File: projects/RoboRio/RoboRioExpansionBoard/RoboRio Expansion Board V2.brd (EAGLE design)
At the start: 56.6 x 77.5 mm, 125 parts, among them J1 RRINTERFACE-FEMALE, J10 SPI_MISO, J11 SPI_MOSI, J12 I2C_SCL, J13 I2C_SDA, J14 UART_TX, J15 UART_RX, J16 LCD, J17 ADC1, J18 ADC2, J19 ADC3, J2 MICROSD-HINGED, J20 ADC4, J21 ADC5, J22 ADC6, J23 ADC7, J25 PWM0, J26 PWM1, J27 PWM2, J28 PWM3, J29 PWM4, J3 51387-0578, J30 PWM5, J31 PWM6, J32 PWM7, J33 PWM8, J34 PWM9, J35 AI0, J36 AI1, J37 AI2, J38 AI3, J39 AO0, J4 GPIO0, J40 AO1, J5 GPIO1, J6 GPIO2, J7 GPIO3, J8 SPI_CS, J9 SPI_CLK, Q1 NPN-SOT416, Q2 NPN-SOT416, Q3 NPN-SOT416, U1 P8X32A-Q44_P, U2 24LC256ST, U3 FT232RL, U4 TC54VN43, U5 TPS2115APWR, U6 REG1117, U7 ADC124S01, U8 ADC124S01, Y1 5MHz

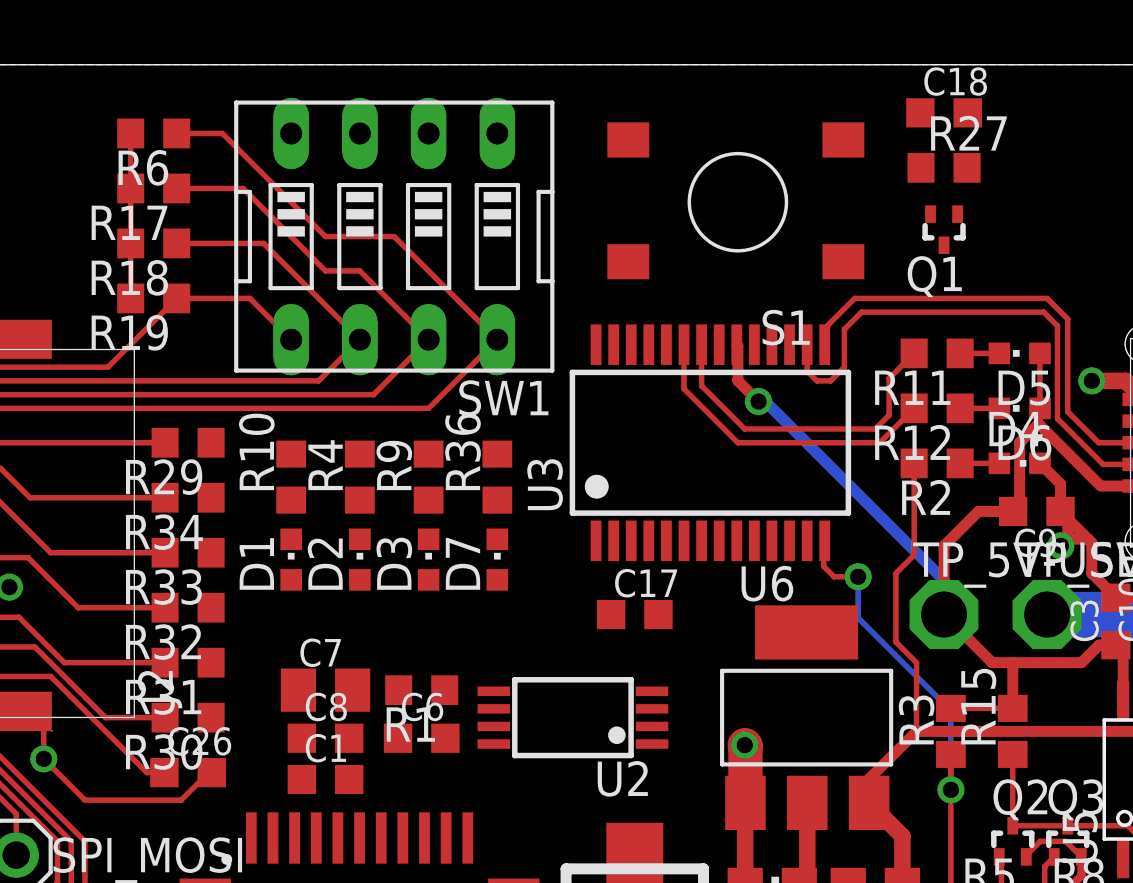
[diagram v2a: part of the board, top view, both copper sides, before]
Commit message: Fixed a few small issues
Also connected reset button.
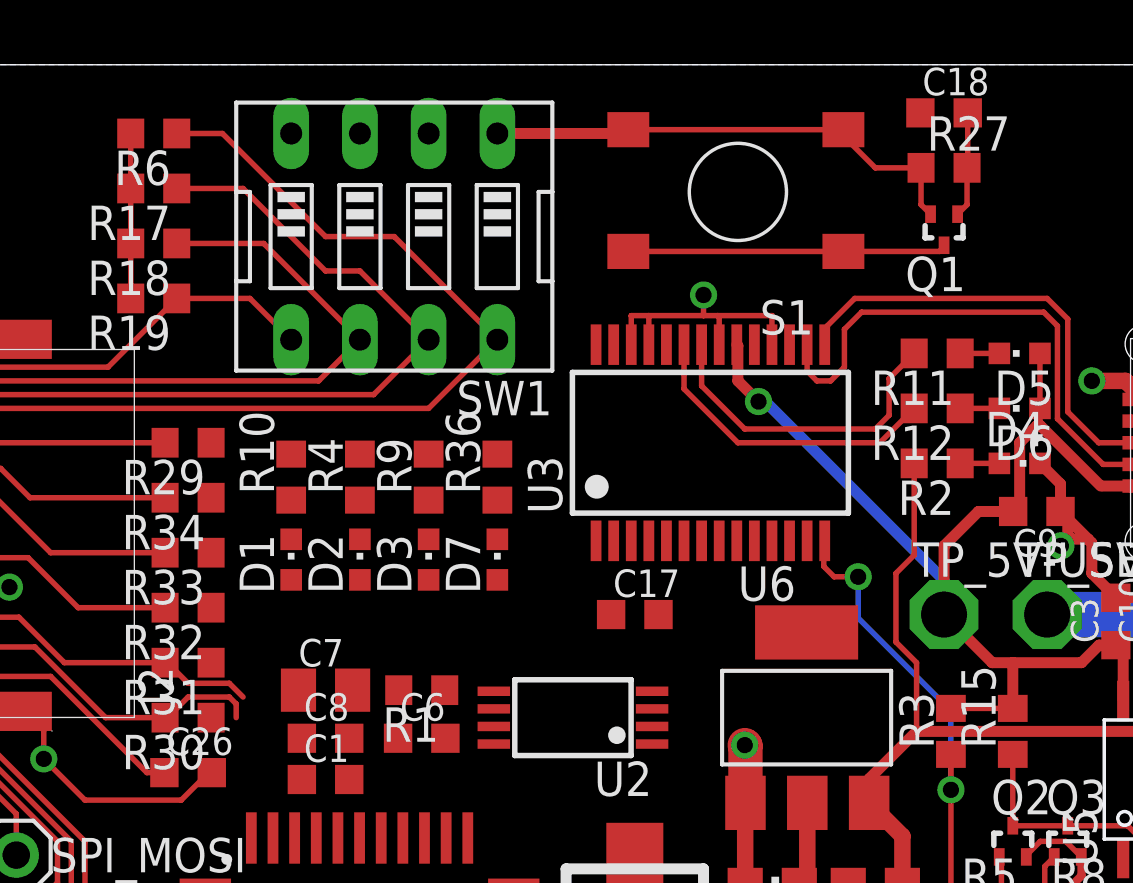
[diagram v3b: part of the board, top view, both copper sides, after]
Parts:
- moved S1 0.38 mm to (36.8, 72.8)
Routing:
- net DGND: track 75.9 -> 104.5 mm, vias 7 -> 8
- net !RESET: track 0.00 -> 11.8 mm
- net N$26: track 0.00 -> 3.90 mm
- net IO0: track 8.87 -> 12.4 mm
- net IO1: track 8.48 -> 11.9 mm
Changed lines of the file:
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@@
 <element name="U8" library="adc124s021cimm" package="ADC124S021VSSOP" value="ADC124S01" x="36.068" y="32.512"/>
 <element name="Y1" library="crystalsmt" package="HC\49US" value="5MHz" x="33.02" y="41.91" rot="R270"/>
-<element name="S1" library="resetbutton9001" package="RESETBUTTON9001" value="RESETBUTTON9001DEFAULT" x="36.83" y="72.39" rot="R180"/>
+<element name="S1" library="resetbutton9001" package="RESETBUTTON9001" value="RESETBUTTON9001DEFAULT" x="36.83" y="72.771" rot="R180"/>
 </elements>
 <signals>
@@
 <contactref element="S1" pad="2"/>
 <contactref element="S1" pad="1"/>
-<wire x1="40.73" y1="70.19" x2="44.45" y2="70.799" width="0" layer="19" extent="1-1"/>
-<wire x1="32.78" y1="70.19" x2="40.73" y2="70.19" width="0" layer="19" extent="1-1"/>
-<wire x1="17.1475" y1="42.3925" x2="32.78" y2="70.19" width="0" layer="19" extent="1-1"/>
+<wire x1="44.45" y1="70.799" x2="44.45" y2="70.739" width="0.2032" layer="1"/>
+<wire x1="44.45" y1="70.739" x2="44.282" y2="70.571" width="0.2032" layer="1"/>
+<wire x1="44.282" y1="70.571" x2="40.73" y2="70.571" width="0.2032" layer="1"/>
+<wire x1="40.73" y1="70.571" x2="32.78" y2="70.571" width="0.2032" layer="1"/>
+<wire x1="17.1475" y1="42.3925" x2="32.78" y2="70.571" width="0" layer="19" extent="1-1"/>
 </signal>
 <signal name="IO5">
@@
 <wire x1="37.084" y1="52.324" x2="37.1094" y2="52.2986" width="1.27" layer="1"/>
 <wire x1="37.1094" y1="52.2986" x2="37.1094" y2="50.1904" width="1.27" layer="1"/>
-<wire x1="43.95" y1="71.949" x2="43.6" y2="73.66" width="0" layer="19" extent="1-1"/>
-<wire x1="40.73" y1="74.69" x2="43.6" y2="73.66" width="0" layer="19" extent="1-1"/>
-<wire x1="38.089" y1="67.125" x2="43.95" y2="71.949" width="0" layer="19" extent="1-1"/>
-<wire x1="36.139" y1="67.125" x2="38.089" y2="67.125" width="0" layer="19" extent="1-1"/>
-<wire x1="33.539" y1="67.125" x2="36.139" y2="67.125" width="0" layer="19" extent="1-1"/>
-<wire x1="32.889" y1="67.125" x2="33.539" y2="67.125" width="0" layer="19" extent="1-1"/>
-<wire x1="27.94" y1="63.08" x2="32.889" y2="67.125" width="0" layer="19" extent="1-1"/>
-<wire x1="25.4" y1="63.08" x2="27.94" y2="63.08" width="0" layer="19" extent="1-1"/>
-<wire x1="22.86" y1="63.08" x2="25.4" y2="63.08" width="0" layer="19" extent="1-1"/>
-<wire x1="20.32" y1="63.08" x2="22.86" y2="63.08" width="0" layer="19" extent="1-1"/>
-<wire x1="32.145" y1="57.15" x2="27.94" y2="63.08" width="0" layer="19" extent="1-1"/>
-<wire x1="33.659" y1="54.315" x2="32.145" y2="57.15" width="0" layer="19" extent="1-1"/>
-<wire x1="33.659" y1="53.665" x2="33.659" y2="54.315" width="0" layer="19" extent="1-1"/>
-<wire x1="33.659" y1="53.015" x2="33.659" y2="53.665" width="0" layer="19" extent="1-1"/>
-<wire x1="33.659" y1="52.365" x2="33.659" y2="53.015" width="0" layer="19" extent="1-1"/>
-<wire x1="37.084" y1="52.324" x2="33.659" y2="52.365" width="0" layer="19" extent="1-1"/>
+<wire x1="32.889" y1="67.125" x2="32.889" y2="68.195" width="0.2032" layer="1"/>
+<wire x1="32.889" y1="68.195" x2="32.893" y2="68.199" width="0.2032" layer="1"/>
+<wire x1="32.893" y1="68.199" x2="33.528" y2="68.199" width="0.2032" layer="1"/>
+<wire x1="33.528" y1="68.199" x2="35.56" y2="68.199" width="0.2032" layer="1"/>
+<wire x1="36.083" y1="68.199" x2="38.1" y2="68.199" width="0.2032" layer="1"/>
+<wire x1="33.539" y1="67.125" x2="33.539" y2="68.188" width="0.2032" layer="1"/>
+<wire x1="33.539" y1="68.188" x2="33.528" y2="68.199" width="0.2032" layer="1"/>
+<wire x1="36.139" y1="67.125" x2="36.139" y2="68.143" width="0.2032" layer="1"/>
+<wire x1="38.089" y1="67.125" x2="38.089" y2="68.188" width="0.2032" layer="1"/>
+<wire x1="38.089" y1="68.188" x2="38.1" y2="68.199" width="0.2032" layer="1"/>
+<wire x1="40.73" y1="75.071" x2="40.73" y2="74.84" width="0.2032" layer="1"/>
+<wire x1="40.73" y1="74.84" x2="41.91" y2="73.66" width="0.2032" layer="1"/>
+<wire x1="41.91" y1="73.66" x2="43.6" y2="73.66" width="0.2032" layer="1"/>
+<wire x1="43.6" y1="73.66" x2="43.6" y2="72.299" width="0.2032" layer="1"/>
+<wire x1="43.6" y1="72.299" x2="43.95" y2="71.949" width="0.2032" layer="1"/>
+<wire x1="32.78" y1="75.071" x2="40.73" y2="75.071" width="0.2032" layer="1"/>
+<wire x1="27.94" y1="74.93" x2="32.639" y2="74.93" width="0.4064" layer="1"/>
+<wire x1="32.639" y1="74.93" x2="32.78" y2="75.071" width="0.4064" layer="1"/>
+<via x="35.56" y="68.961" extent="1-16" drill="0.6" shape="square"/>
+<wire x1="35.56" y1="68.199" x2="35.56" y2="68.961" width="0.2032" layer="1"/>
 <wire x1="52.37" y1="48.154" x2="49.53" y2="48.185" width="0" layer="19" extent="1-1"/>
+<wire x1="33.659" y1="52.365" x2="37.084" y2="52.324" width="0" layer="19" extent="1-1"/>
+<wire x1="33.659" y1="53.015" x2="33.659" y2="52.365" width="0" layer="19" extent="1-1"/>
+<wire x1="33.659" y1="53.665" x2="33.659" y2="53.015" width="0" layer="19" extent="1-1"/>
+<wire x1="33.659" y1="54.315" x2="33.659" y2="53.665" width="0" layer="19" extent="1-1"/>
+<wire x1="32.145" y1="57.15" x2="33.659" y2="54.315" width="0" layer="19" extent="1-1"/>
 <wire x1="40.91" y1="46.99" x2="37.1" y2="46.99" width="0" layer="19" extent="1-1"/>
 <wire x1="35.489" y1="59.875" x2="32.145" y2="57.15" width="0" layer="19" extent="1-1"/>
@@
 <wire x1="39.003" y1="22.86" x2="39.003" y2="25.4" width="0" layer="19" extent="1-1"/>
 <wire x1="39.003" y1="20.32" x2="39.003" y2="22.86" width="0" layer="19" extent="1-1"/>
-<wire x1="32.78" y1="74.69" x2="27.94" y2="74.93" width="0" layer="19" extent="1-1"/>
 <wire x1="44.03" y1="38.1" x2="39.003" y2="38.1" width="0" layer="19" extent="1-1"/>
 <wire x1="22.465" y1="51.054" x2="17.385" y2="51.308" width="0" layer="19" extent="1-1"/>
@@
 <wire x1="17.1475" y1="43.9925" x2="16.256" y2="50.292" width="0" layer="19" extent="1-1"/>
 <wire x1="17.1475" y1="43.1925" x2="17.1475" y2="43.9925" width="0" layer="19" extent="1-1"/>
+<wire x1="27.94" y1="63.08" x2="32.889" y2="67.125" width="0" layer="19" extent="1-1"/>
+<wire x1="25.4" y1="63.08" x2="27.94" y2="63.08" width="0" layer="19" extent="1-1"/>
+<wire x1="22.86" y1="63.08" x2="25.4" y2="63.08" width="0" layer="19" extent="1-1"/>
+<wire x1="20.32" y1="63.08" x2="22.86" y2="63.08" width="0" layer="19" extent="1-1"/>
 <wire x1="22.8475" y1="37.4925" x2="17.1475" y2="43.1925" width="0" layer="19" extent="1-1"/>
 <wire x1="28.5475" y1="42.3925" x2="22.8475" y2="37.4925" width="0" layer="19" extent="1-1"/>
+<wire x1="35.56" y1="68.199" x2="36.083" y2="68.199" width="0.2032" layer="1"/>
+<wire x1="36.083" y1="68.199" x2="36.139" y2="68.143" width="0.2032" layer="1"/>
 </signal>
 <signal name="N$8">
@@
 <wire x1="10.85" y1="55.952" x2="13.462" y2="53.34" width="0.2032" layer="1"/>
 <wire x1="13.462" y1="53.34" x2="15.66" y2="53.34" width="0.2032" layer="1"/>
-<wire x1="15.66" y1="53.34" x2="21.2475" y2="48.8925" width="0" layer="19" extent="1-1"/>
+<wire x1="15.66" y1="53.34" x2="15.748" y2="53.34" width="0.2032" layer="1"/>
+<wire x1="15.748" y1="53.34" x2="16.51" y2="54.102" width="0.2032" layer="1"/>
+<wire x1="16.51" y1="54.102" x2="18.034" y2="54.102" width="0.2032" layer="1"/>
+<wire x1="18.034" y1="54.102" x2="18.288" y2="53.848" width="0.2032" layer="1"/>
+<wire x1="18.288" y1="53.848" x2="18.288" y2="53.34" width="0.2032" layer="1"/>
+<wire x1="18.288" y1="53.34" x2="21.2475" y2="48.8925" width="0" layer="19" extent="1-1"/>
 </signal>
 <signal name="IO1">
@@
 <wire x1="11.938" y1="55.372" x2="10.258" y2="57.052" width="0.2032" layer="1"/>
 <wire x1="10.258" y1="57.052" x2="7.874" y2="57.052" width="0.2032" layer="1"/>
-<wire x1="15.66" y1="55.372" x2="20.4475" y2="48.8925" width="0" layer="19" extent="1-1"/>
+<wire x1="15.66" y1="55.372" x2="15.748" y2="55.372" width="0.2032" layer="1"/>
+<wire x1="15.748" y1="55.372" x2="16.51" y2="54.61" width="0.2032" layer="1"/>
+<wire x1="16.51" y1="54.61" x2="18.034" y2="54.61" width="0.2032" layer="1"/>
+<wire x1="18.034" y1="54.61" x2="18.542" y2="54.102" width="0.2032" layer="1"/>
+<wire x1="18.542" y1="54.102" x2="20.4475" y2="48.8925" width="0" layer="19" extent="1-1"/>
 </signal>
 <signal name="IO2">
@@
 <contactref element="C18" pad="2"/>
 <contactref element="Q1" pad="1"/>
-<wire x1="44.95" y1="71.949" x2="45.3" y2="73.66" width="0" layer="19" extent="1-1"/>
-<wire x1="45.325" y1="75.692" x2="45.3" y2="73.66" width="0" layer="19" extent="1-1"/>
+<wire x1="45.325" y1="75.692" x2="45.325" y2="73.685" width="0.2032" layer="1"/>
+<wire x1="45.325" y1="73.685" x2="45.3" y2="73.66" width="0.2032" layer="1"/>
+<wire x1="45.3" y1="73.66" x2="45.3" y2="72.299" width="0.2032" layer="1"/>
+<wire x1="45.3" y1="72.299" x2="44.95" y2="71.949" width="0.2032" layer="1"/>
 </signal>
 <signal name="N$32">

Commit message: Connected D3 to the proper IO pin.
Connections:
- net IO16: now also D3.A
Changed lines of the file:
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@@
 <signal name="IO16">
 <contactref element="U1" pad="19"/>
+<contactref element="D3" pad="A"/>
+<wire x1="24.4475" y1="37.4925" x2="25.4" y2="58.432" width="0" layer="19" extent="1-1"/>
 </signal>
 <signal name="IO17">
@@
 <via x="35.56" y="68.961" extent="1-16" drill="0.6" shape="square"/>
 <wire x1="35.56" y1="68.199" x2="35.56" y2="68.961" width="0.2032" layer="1"/>
-<wire x1="52.37" y1="48.154" x2="49.53" y2="48.185" width="0" layer="19" extent="1-1"/>
+<wire x1="35.56" y1="68.199" x2="36.083" y2="68.199" width="0.2032" layer="1"/>
+<wire x1="36.083" y1="68.199" x2="36.139" y2="68.143" width="0.2032" layer="1"/>
+<wire x1="49.53" y1="48.185" x2="52.37" y2="48.154" width="0" layer="19" extent="1-1"/>
 <wire x1="33.659" y1="52.365" x2="37.084" y2="52.324" width="0" layer="19" extent="1-1"/>
 <wire x1="33.659" y1="53.015" x2="33.659" y2="52.365" width="0" layer="19" extent="1-1"/>
@@
 <wire x1="22.8475" y1="37.4925" x2="17.1475" y2="43.1925" width="0" layer="19" extent="1-1"/>
 <wire x1="28.5475" y1="42.3925" x2="22.8475" y2="37.4925" width="0" layer="19" extent="1-1"/>
-<wire x1="35.56" y1="68.199" x2="36.083" y2="68.199" width="0.2032" layer="1"/>
-<wire x1="36.083" y1="68.199" x2="36.139" y2="68.143" width="0.2032" layer="1"/>
 </signal>
 <signal name="N$8">

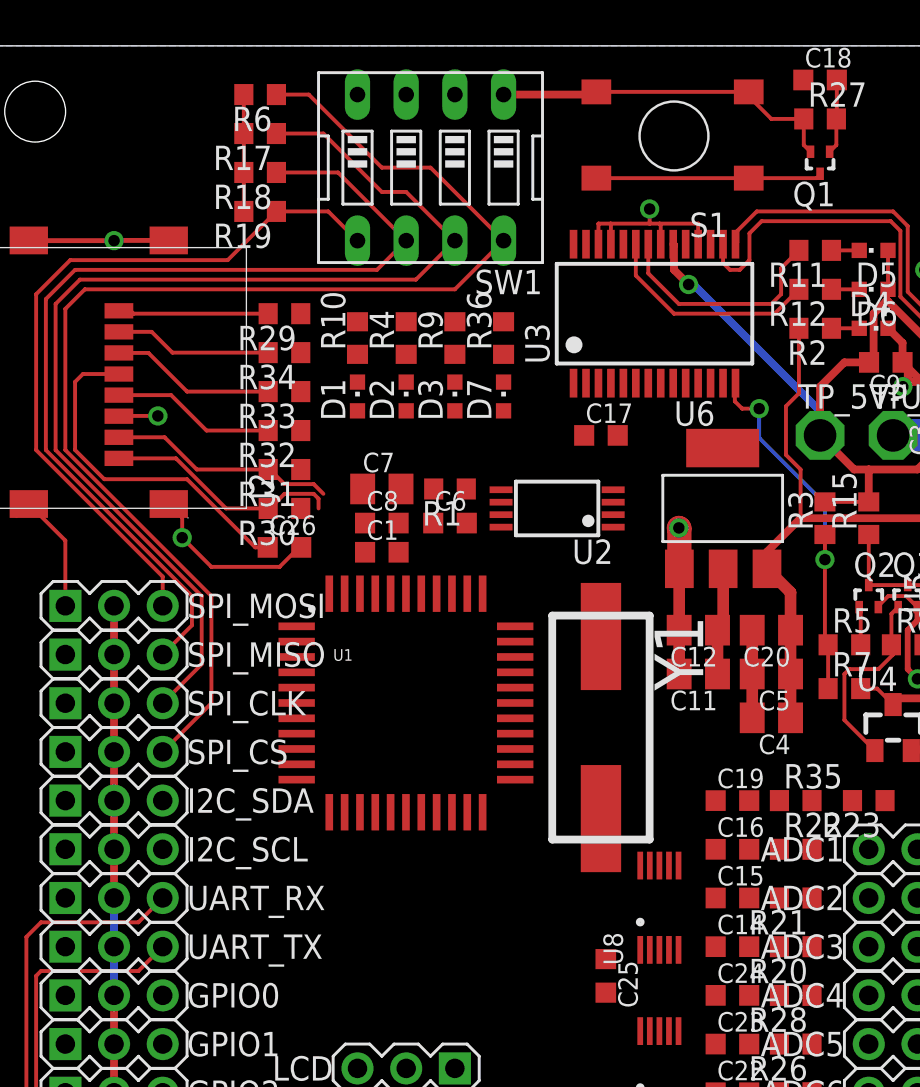
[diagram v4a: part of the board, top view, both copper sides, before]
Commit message: Opened routing to the SD card.
+3v3 is now connected to all pullup resistors.
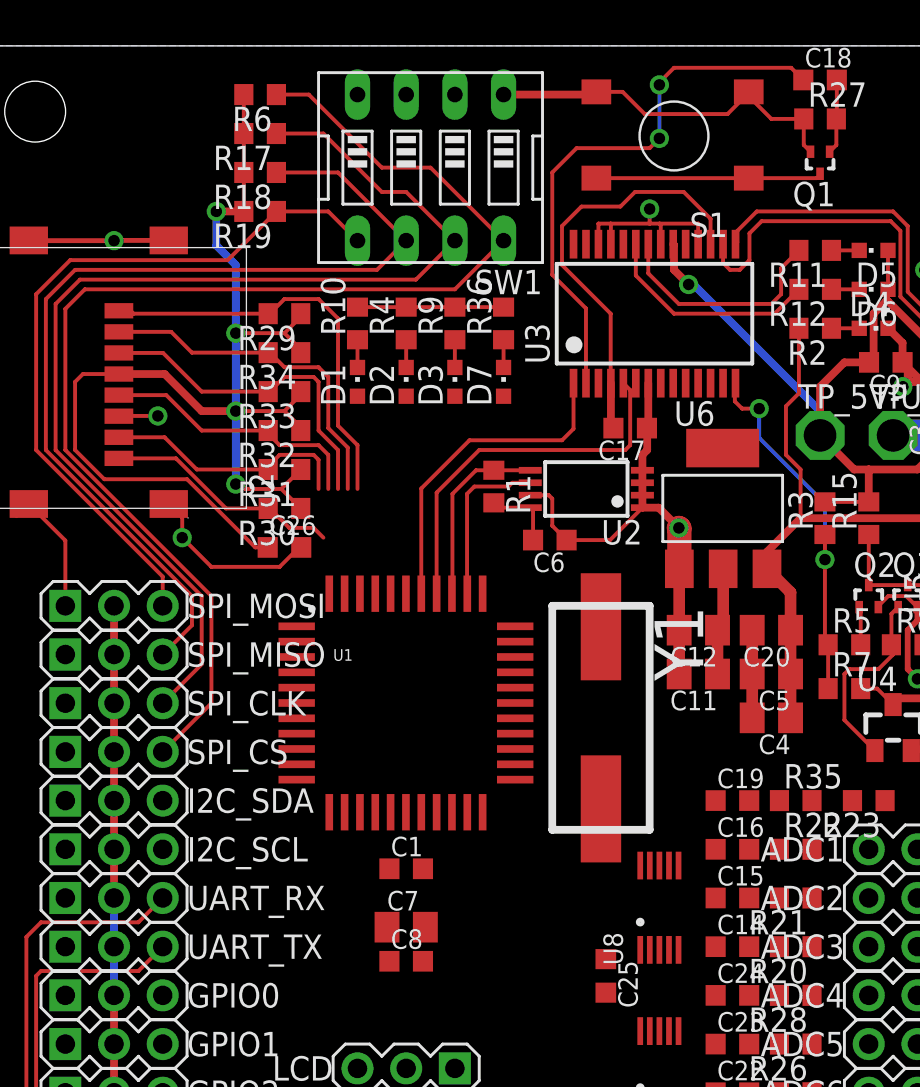
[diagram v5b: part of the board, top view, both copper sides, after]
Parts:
- moved C7 22.9 mm to (22.9, 31.5)
- moved C8 22.9 mm to (22.9, 29.7)
- moved C1 16.6 mm to (22.9, 34.5)
- moved C6 5.28 mm to (30.4, 51.7), turned to 180 degrees
- moved R1 2.29 mm to (27.4, 54.5), turned to 270 degrees
- moved U2 1.83 mm to (32.3, 54.4)
- moved C17 1.57 mm to (34.5, 57.5), turned to 180 degrees
- moved D1 0.76 mm to (20.3, 59.9)
- moved D2 0.76 mm to (22.9, 59.9)
- moved D3 0.76 mm to (25.4, 59.9)
- moved D7 0.76 mm to (27.9, 59.9)
- moved R10 0.76 mm to (20.3, 63.0)
- moved R36 0.76 mm to (27.9, 63.0)
- moved R4 0.76 mm to (22.9, 63.0)
- moved R9 0.76 mm to (25.4, 63.0)
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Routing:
- net +3V3: track 57.8 -> 100.8 mm, vias 0 -> 4
- net N$19: track 0.00 -> 29.1 mm, vias 0 -> 2
- net DGND: track 104.5 -> 130.8 mm
- net N$3: track 0.00 -> 22.0 mm
- net IO30_TX: track 0.00 -> 19.8 mm
- net IO31_RX: track 0.00 -> 17.1 mm
- net IO25: track 7.85 -> 21.5 mm
- net IO27: track 8.24 -> 18.2 mm
- net IO29_SDA: track 0.00 -> 9.79 mm
- net IO3: track 8.62 -> 17.7 mm
- net IO28_SCL: track 0.00 -> 8.75 mm
- net IO2: track 8.55 -> 14.1 mm
- net N$17: track 0.00 -> 1.45 mm
- net N$14: track 0.00 -> 1.45 mm
- net N$13: track 0.00 -> 1.45 mm
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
